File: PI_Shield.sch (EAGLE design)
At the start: 78 parts, among them J10 T2I, J11 T2I, J12 T2I, J13 DF13-4P-1.25DSA, J14 DF13-4P-1.25DSA, J15 DF13-4P-1.25DSA, J16 T2I5P, J17 USB-MICRO, Q1 220mA/50V/3.5Ω, Q2 220mA/50V/3.5Ω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

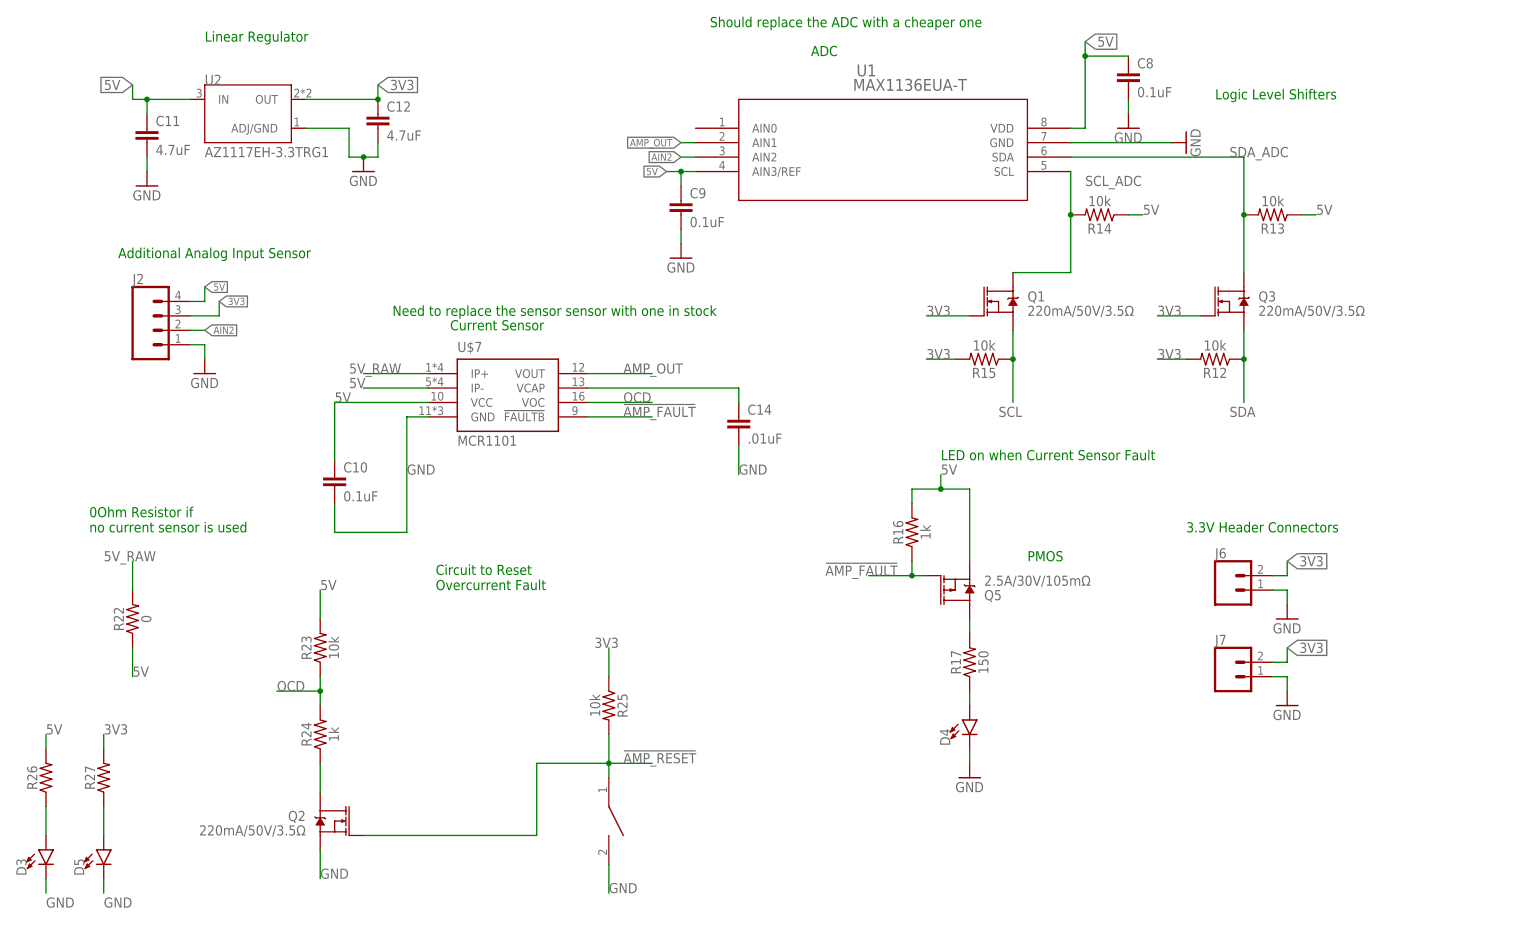
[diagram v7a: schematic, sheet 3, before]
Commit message: Added more notes to schematic
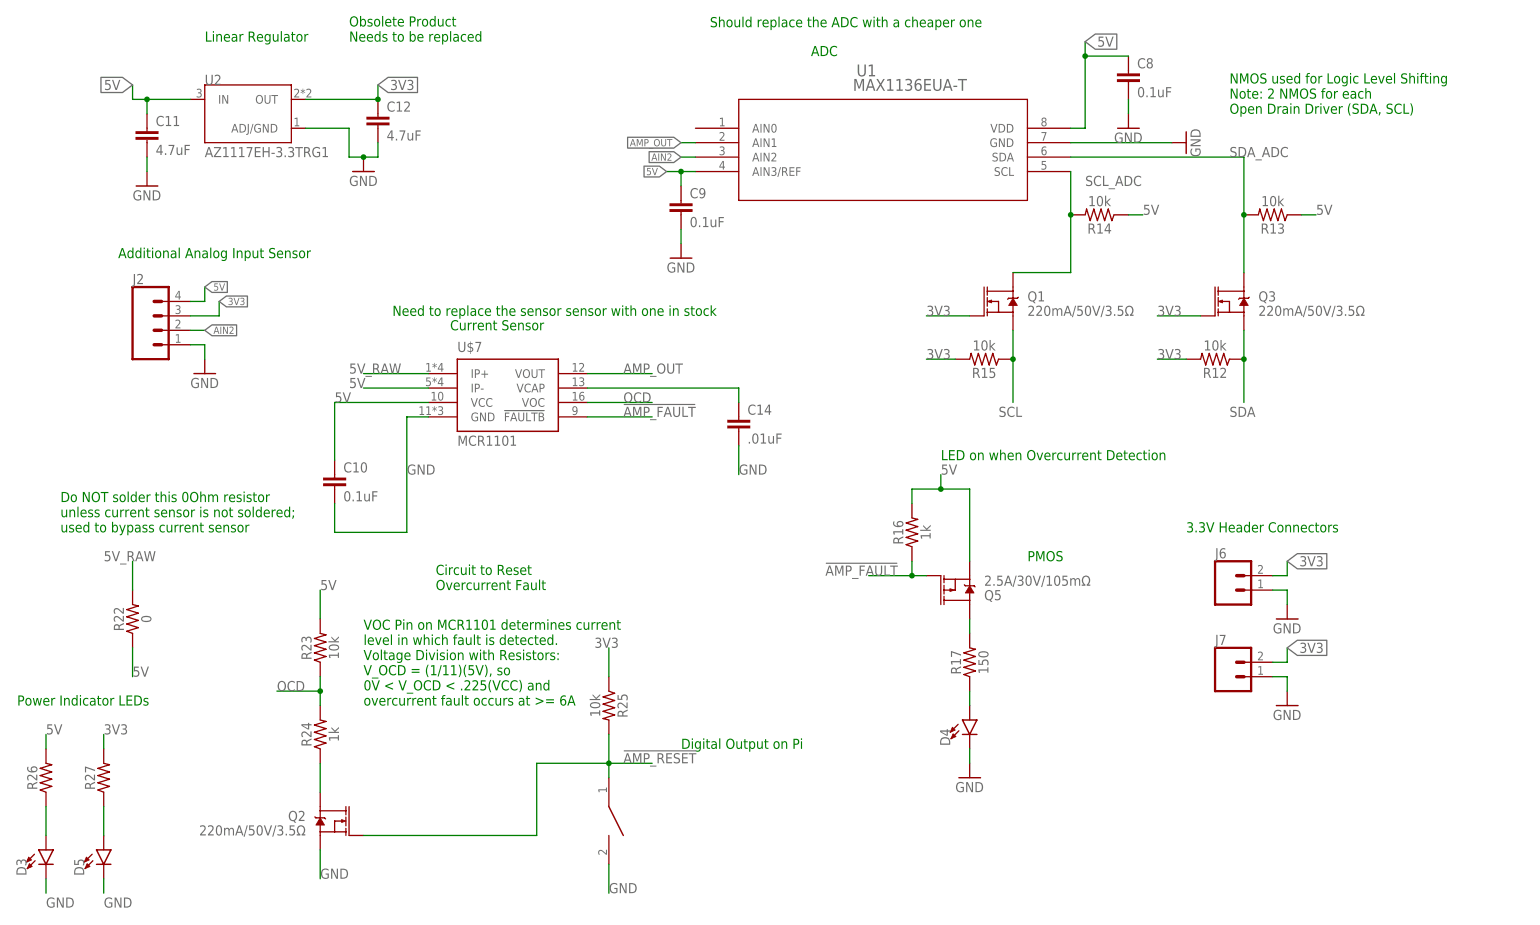
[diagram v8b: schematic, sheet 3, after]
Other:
- note added: "Digital Output on Pi"
- note added: "Do NOT solder this 0Ohm resistor unless current sensor is not soldered; used to bypass current sensor"
- note added: "LED on when Overcurrent Detection"
- note added: "LED turns on when CAN Tranceiver detects a fault"
- note added: "NMOS used for Logic Level Shifting Note: 2 NMOS for each Open Drain Driver (SDA, SCL)"
- note added: "Note: Same CS as connected to CAN Controller MCP2515"
- note added: "Obsolete Product Needs to be replaced"
- note added: "Only pull ADR high if wanting to change address from 0x28 to 0x29; use 0Ohm to do so, as breakout board has a pull down resistor"
- note added: "Oscillator ECS-80-18-4X"
- note added: "Power Indicator LEDs"
- note added: "VOC Pin on MCR1101 determines current level in which fault is detected. Voltage Division with Resistors: V_OCD = (1/11)(5V), so 0V < V_OCD < .225(VCC) and overcurrent fault occurs at >= 6A"
- note removed: "0Ohm Resistor if no current sensor is used"
- note removed: "LED on when Current Sensor Fault"
- note removed: "Logic Level Shifters"
- note removed: "Only pull ADR high if wanting to change address from 0x28 to 0x29"
- note removed: "Oscillator"
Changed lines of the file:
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@@
 <sheet>
 <plain>
-<text x="40.64" y="58.42" size="1.778" layer="91">Oscillator</text>
+<text x="40.64" y="58.42" size="1.778" layer="91">Oscillator
+ECS-80-18-4X</text>
 <text x="203.2" y="149.86" size="1.778" layer="91">CAN Termination</text>
 <text x="213.36" y="88.9" size="1.778" layer="91">CAN to MiniROV Connectors</text>
@@
 Silent mode is unwanted
 Do not populate R3</text>
+<text x="147.32" y="91.44" size="1.778" layer="91">LED turns on when CAN Tranceiver detects a fault</text>
 </plain>
 <instances>
@@
 <text x="129.54" y="27.94" size="1.778" layer="91">UART Communication Header Pins</text>
 <text x="210.82" y="68.58" size="1.778" layer="91">Servo Connector</text>
-<text x="223.52" y="121.92" size="1.778" layer="91">Only pull ADR high if wanting
+<text x="228.6" y="116.84" size="1.778" layer="91">Only pull ADR high if wanting
 to change address from
-0x28 to 0x29</text>
+0x28 to 0x29;
+use 0Ohm to do so, as breakout board
+has a pull down resistor</text>
 <text x="132.08" y="162.56" size="1.778" layer="91">Use same decoupling cap as BNO055</text>
 <text x="175.26" y="134.62" size="1.778" layer="91">I2C Pull-up Resistors</text>
+<text x="172.72" y="50.8" size="1.778" layer="91">Note: Same CS as connected to
+CAN Controller MCP2515</text>
 </plain>
 <instances>
@@
 <text x="213.36" y="73.66" size="1.778" layer="91">3.3V Header Connectors</text>
 <text x="185.42" y="68.58" size="1.778" layer="91">PMOS</text>
-<text x="170.18" y="86.36" size="1.778" layer="91">LED on when Current Sensor Fault</text>
-<text x="218.44" y="149.86" size="1.778" layer="91">Logic Level Shifters</text>
+<text x="170.18" y="86.36" size="1.778" layer="91">LED on when Overcurrent Detection</text>
+<text x="220.98" y="147.32" size="1.778" layer="91">NMOS used for Logic Level Shifting
+Note: 2 NMOS for each
+Open Drain Driver (SDA, SCL)</text>
 <text x="40.64" y="160.02" size="1.778" layer="91">Linear Regulator</text>
-<text x="20.32" y="73.66" size="1.778" layer="91">0Ohm Resistor if
-no current sensor is used</text>
+<text x="15.24" y="73.66" size="1.778" layer="91">Do NOT solder this 0Ohm resistor
+unless current sensor is not soldered;
+used to bypass current sensor</text>
 <text x="83.82" y="109.22" size="1.778" layer="91">Current Sensor</text>
 <text x="81.28" y="63.5" size="1.778" layer="91">Circuit to Reset
@@
 <text x="73.66" y="111.76" size="1.778" layer="91">Need to replace the sensor sensor with one in stock</text>
 <text x="129.54" y="162.56" size="1.778" layer="91">Should replace the ADC with a cheaper one</text>
+<text x="66.04" y="160.02" size="1.778" layer="91">Obsolete Product
+Needs to be replaced</text>
+<text x="7.62" y="43.18" size="1.778" layer="91">Power Indicator LEDs</text>
+<text x="68.58" y="43.18" size="1.778" layer="91">VOC Pin on MCR1101 determines current
+level in which fault is detected.
+Voltage Division with Resistors:
+V_OCD = (1/11)(5V), so
+0V &lt; V_OCD &lt; .225(VCC) and
+overcurrent fault occurs at &gt;= 6A</text>
+<text x="124.46" y="35.56" size="1.778" layer="91">Digital Output on Pi</text>
 </plain>
 <instances>
